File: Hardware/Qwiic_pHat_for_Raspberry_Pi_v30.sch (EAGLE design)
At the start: 28 parts, among them J1 RASPBERRYPI-40-PIN-GPIO_PTH_N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, J4 Qwiic Right Angle, J7 Qwiic Right Angle

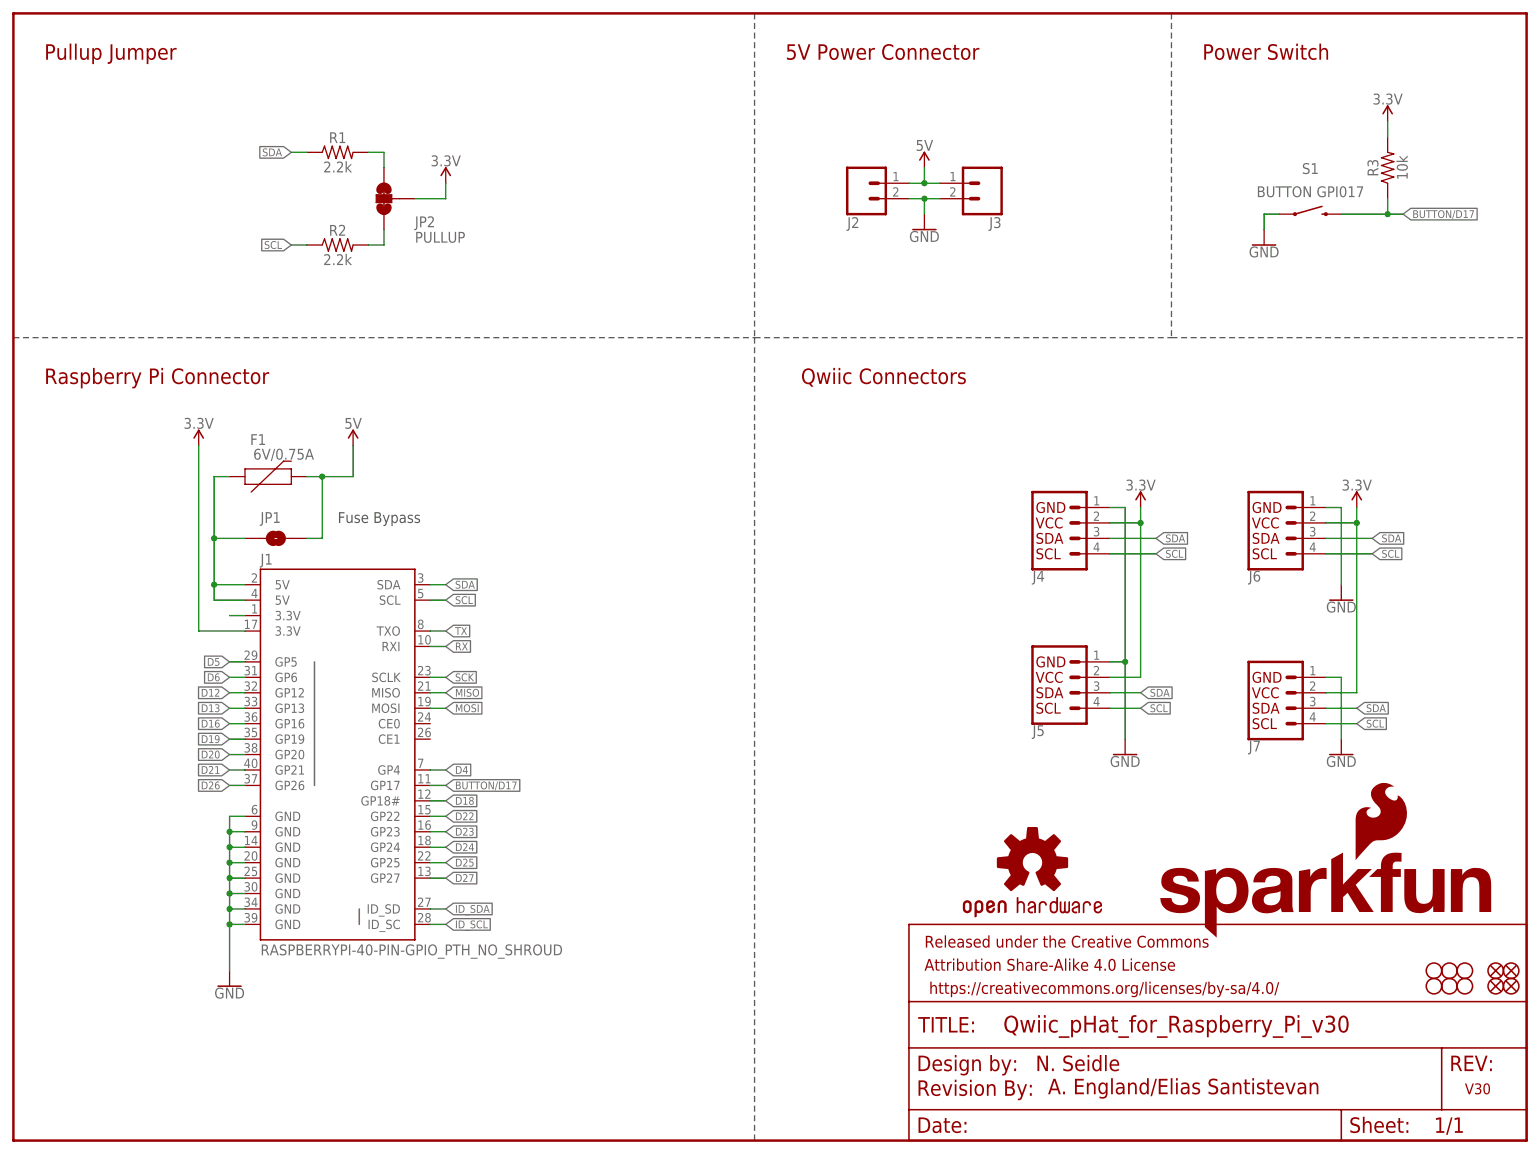
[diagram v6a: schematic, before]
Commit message: Swaps power and ground on screw terminal, adjusts silk in various areas
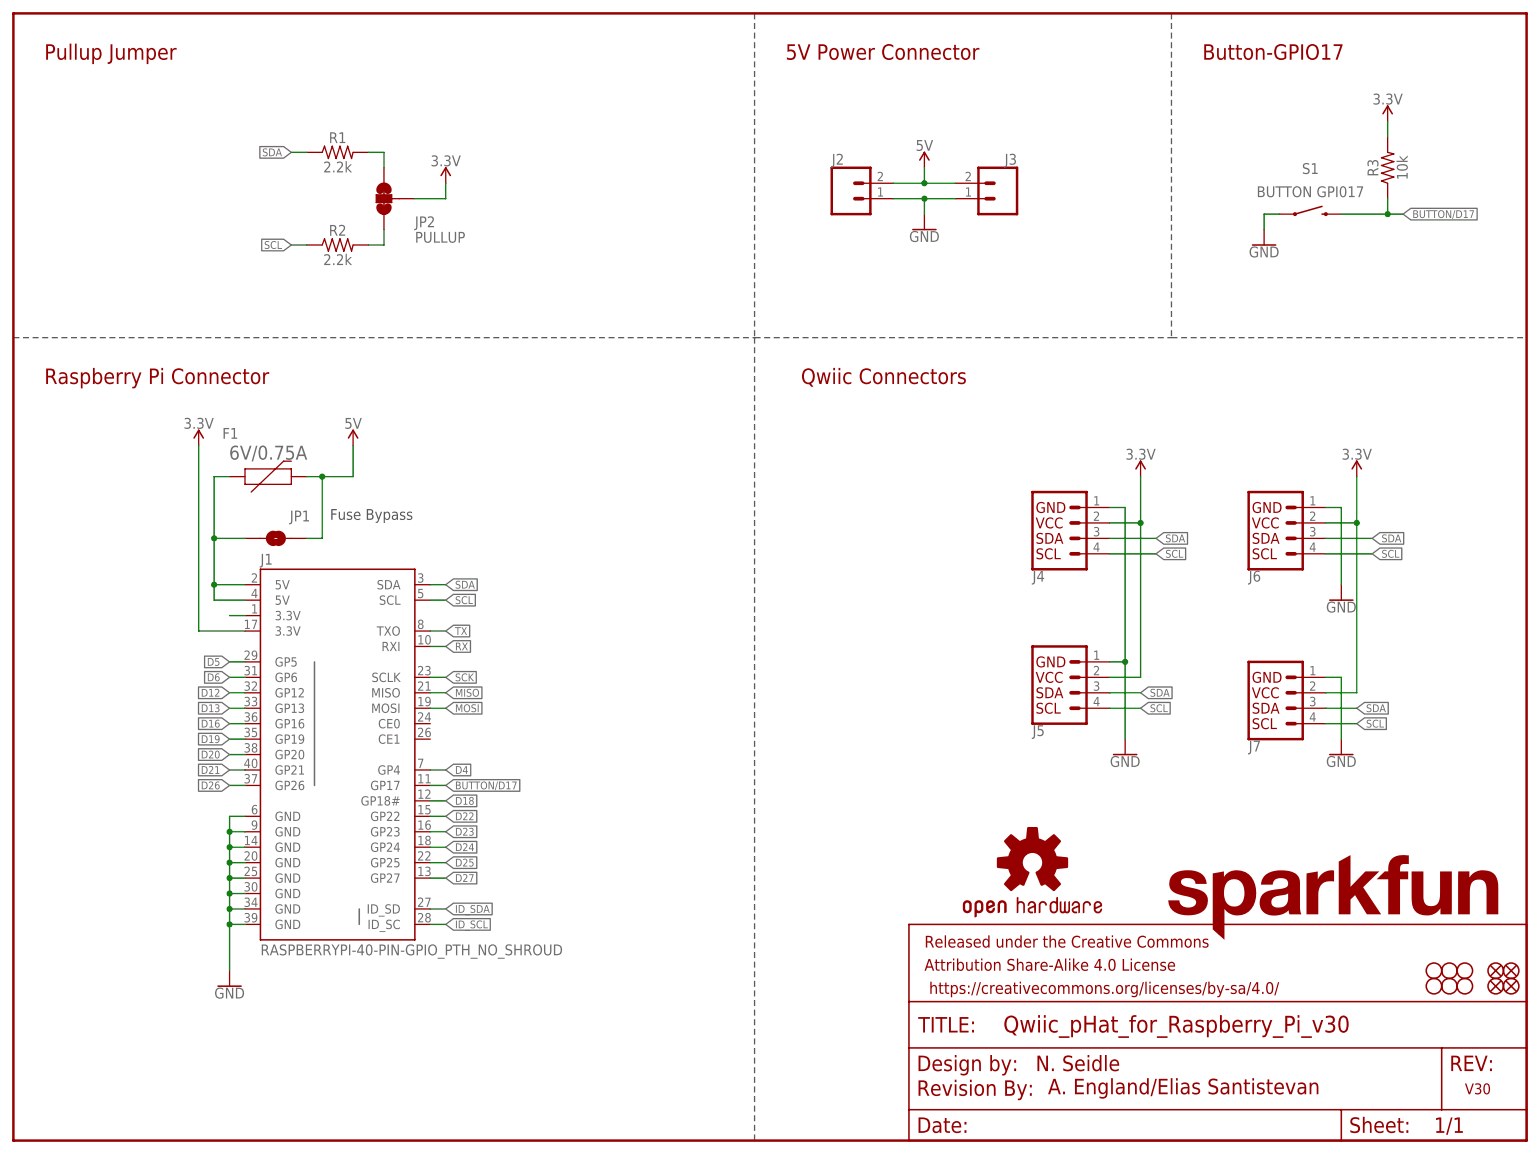
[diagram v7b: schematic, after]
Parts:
- LOGO3: value SFE_LOGO_NAME_FLAME.1_INCH -> SFE_LOGO_NAME.1_INCH; device SparkFun-Aesthetics:SFE_LOGO_NAME_FLAME.1_INCH -> SparkFun-Aesthetics:SFE_LOGO_NAME.1_INCH
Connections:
- net 5V: now also J2.2, J3.2; no longer J2.1, J3.1
- net GND: now also J2.1, J3.1; no longer J2.2, J3.2
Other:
- note added: "Button-GPIO17"
- note removed: "Power Switch"
- moved on the sheet: J2, J3
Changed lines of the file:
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@@
 <part name="H3" library="SparkFun-Hardware" deviceset="STAND-OFF" device="TIGHT"/>
 <part name="H2" library="SparkFun-Hardware" deviceset="STAND-OFF" device="TIGHT"/>
-<part name="LOGO3" library="SparkFun-Aesthetics" deviceset="SFE_LOGO_NAME_FLAME" device=".1_INCH" value="SFE_LOGO_NAME_FLAME.1_INCH"/>
 <part name="LOGO2" library="SparkFun-Aesthetics" deviceset="OSHW-LOGO" device="S" value="OSHW-LOGOS"/>
 <part name="JP2" library="SparkFun-Jumpers" deviceset="JUMPER-SMT_3_2-NC_TRACE" device="_NO-SILK" value="PULLUP"/>
@@
 <part name="F1" library="SparkFun-Fuses" deviceset="PPTC" device="_0.75A" value="6V/0.75A"/>
 <part name="JP1" library="SparkFun-Jumpers" deviceset="JUMPER-SMT_2_NO" device="_SILK" value="JUMPER-SMT_2_NO_SILK"/>
+<part name="LOGO3" library="SparkFun-Aesthetics" deviceset="SFE_LOGO_NAME" device=".1_INCH" value="SFE_LOGO_NAME.1_INCH"/>
 </parts>
 <sheets>
@@
 <wire x1="190.5" y1="132.08" x2="248.92" y2="132.08" width="0.2032" layer="97" style="shortdash"/>
 <wire x1="190.5" y1="185.42" x2="190.5" y2="132.08" width="0.2032" layer="97" style="shortdash"/>
-<text x="195.58" y="177.8" size="2.54" layer="94" font="vector" ratio="12">Power Switch</text>
-<text x="53.34" y="101.6" size="1.778" layer="97" font="vector">Fuse Bypass</text>
+<text x="195.58" y="177.8" size="2.54" layer="94" font="vector" ratio="12">Button-GPIO17</text>
+<text x="52.07" y="102.108" size="1.778" layer="97" font="vector">Fuse Bypass</text>
 </plain>
 <instances>
@@
 <attribute name="NAME" x="167.64" y="93.726" size="1.778" layer="95" font="vector" rot="MR180"/>
 </instance>
-<instance part="SUPPLY5" gate="G$1" x="185.42" y="104.14" smashed="yes">
-<attribute name="VALUE" x="185.42" y="106.934" size="1.778" layer="96" align="bottom-center"/>
+<instance part="SUPPLY5" gate="G$1" x="185.42" y="109.22" smashed="yes">
+<attribute name="VALUE" x="185.42" y="112.014" size="1.778" layer="96" align="bottom-center"/>
 </instance>
 <instance part="GND3" gate="1" x="182.88" y="63.5" smashed="yes">
@@
 <instance part="H3" gate="G$1" x="236.22" y="27.94" smashed="yes"/>
 <instance part="H2" gate="G$1" x="233.68" y="25.4" smashed="yes"/>
-<instance part="LOGO3" gate="G$1" x="187.96" y="33.02" smashed="yes"/>
 <instance part="LOGO2" gate="G$1" x="167.64" y="45.72" smashed="yes"/>
 <instance part="JP2" gate="G$1" x="60.96" y="154.94" smashed="yes" rot="R180">
@@
 <attribute name="VALUE" x="30.48" y="117.094" size="1.778" layer="96" align="bottom-center"/>
 </instance>
-<instance part="J3" gate="G$1" x="160.02" y="157.48" smashed="yes" rot="R180">
-<attribute name="VALUE" x="162.56" y="162.306" size="1.778" layer="96" font="vector" rot="R180"/>
-<attribute name="NAME" x="162.56" y="151.892" size="1.778" layer="95" font="vector" rot="R180"/>
+<instance part="J3" gate="G$1" x="162.56" y="154.94" smashed="yes" rot="MR0">
+<attribute name="VALUE" x="165.1" y="150.114" size="1.778" layer="96" font="vector" rot="MR0"/>
+<attribute name="NAME" x="165.1" y="160.528" size="1.778" layer="95" font="vector" rot="MR0"/>
 </instance>
 <instance part="GND2" gate="1" x="149.86" y="149.86" smashed="yes">
@@
 <attribute name="VALUE" x="218.44" y="88.646" size="1.778" layer="96" align="top-center"/>
 </instance>
-<instance part="SUPPLY6" gate="G$1" x="220.98" y="104.14" smashed="yes">
-<attribute name="VALUE" x="220.98" y="106.934" size="1.778" layer="96" align="bottom-center"/>
-</instance>
-<instance part="J2" gate="G$1" x="139.7" y="157.48" smashed="yes" rot="MR180">
-<attribute name="VALUE" x="137.16" y="162.306" size="1.778" layer="96" font="vector" rot="MR180"/>
-<attribute name="NAME" x="137.16" y="151.892" size="1.778" layer="95" font="vector" rot="MR180"/>
+<instance part="SUPPLY6" gate="G$1" x="220.98" y="109.22" smashed="yes">
+<attribute name="VALUE" x="220.98" y="112.014" size="1.778" layer="96" align="bottom-center"/>
+</instance>
+<instance part="J2" gate="G$1" x="137.16" y="154.94" smashed="yes">
+<attribute name="VALUE" x="134.62" y="150.114" size="1.778" layer="96" font="vector"/>
+<attribute name="NAME" x="134.62" y="160.528" size="1.778" layer="95" font="vector"/>
 </instance>
 <instance part="F1" gate="F1" x="40.64" y="109.22" smashed="yes">
-<attribute name="NAME" x="40.259" y="116.205" size="1.778" layer="95" font="vector" rot="R180" align="bottom-center"/>
-<attribute name="VALUE" x="44.45" y="112.014" size="1.778" layer="96" font="vector" rot="R180" align="top-center"/>
+<attribute name="NAME" x="35.687" y="117.221" size="1.778" layer="95" font="vector" rot="R180" align="bottom-center"/>
+<attribute name="VALUE" x="41.91" y="112.014" size="2.286" layer="96" font="vector" rot="R180" align="top-center"/>
 </instance>
 <instance part="JP1" gate="G$1" x="43.18" y="99.06" smashed="yes">
-<attribute name="NAME" x="40.64" y="101.6" size="1.778" layer="95" font="vector"/>
-</instance>
+<attribute name="NAME" x="45.466" y="101.854" size="1.778" layer="95" font="vector"/>
+</instance>
+<instance part="LOGO3" gate="G$1" x="187.96" y="33.02" smashed="yes"/>
 </instances>
 <busses>
@@
 </segment>
 <segment>
-<pinref part="J3" gate="G$1" pin="2"/>
-<wire x1="152.4" y1="154.94" x2="149.86" y2="154.94" width="0.1524" layer="91"/>
-<wire x1="149.86" y1="154.94" x2="149.86" y2="152.4" width="0.1524" layer="91"/>
-<pinref part="GND2" gate="1" pin="GND"/>
-<pinref part="J2" gate="G$1" pin="2"/>
-<wire x1="147.32" y1="154.94" x2="149.86" y2="154.94" width="0.1524" layer="91"/>
-<junction x="149.86" y="154.94"/>
-</segment>
-<segment>
 <pinref part="S1" gate="G$1" pin="1"/>
 <wire x1="208.28" y1="152.4" x2="205.74" y2="152.4" width="0.1524" layer="91"/>
@@
 <pinref part="GND5" gate="1" pin="GND"/>
 </segment>
+<segment>
+<pinref part="J3" gate="G$1" pin="1"/>
+<pinref part="J2" gate="G$1" pin="1"/>
+<wire x1="144.78" y1="154.94" x2="149.86" y2="154.94" width="0.1524" layer="91"/>
+<wire x1="149.86" y1="154.94" x2="154.94" y2="154.94" width="0.1524" layer="91"/>
+<wire x1="149.86" y1="154.94" x2="149.86" y2="152.4" width="0.1524" layer="91"/>
+<junction x="149.86" y="154.94"/>
+<pinref part="GND2" gate="1" pin="GND"/>
+</segment>
 </net>
 <net name="3.3V" class="0">
@@
 <pinref part="J4" gate="G$1" pin="2"/>
 <wire x1="180.34" y1="101.6" x2="185.42" y2="101.6" width="0.1524" layer="91"/>
-<wire x1="185.42" y1="101.6" x2="185.42" y2="104.14" width="0.1524" layer="91"/>
+<wire x1="185.42" y1="101.6" x2="185.42" y2="109.22" width="0.1524" layer="91"/>
 <pinref part="SUPPLY5" gate="G$1" pin="3.3V"/>
 <pinref part="J5" gate="G$1" pin="2"/>
@@
 <pinref part="J6" gate="G$1" pin="2"/>
 <wire x1="215.9" y1="101.6" x2="220.98" y2="101.6" width="0.1524" layer="91"/>
-<wire x1="220.98" y1="101.6" x2="220.98" y2="104.14" width="0.1524" layer="91"/>
+<wire x1="220.98" y1="101.6" x2="220.98" y2="109.22" width="0.1524" layer="91"/>
 <pinref part="SUPPLY6" gate="G$1" pin="3.3V"/>
 <pinref part="J7" gate="G$1" pin="2"/>
@@
 </net>
 <net name="5V" class="0">
-<segment>
-<pinref part="J3" gate="G$1" pin="1"/>
-<wire x1="152.4" y1="157.48" x2="149.86" y2="157.48" width="0.1524" layer="91"/>
-<wire x1="149.86" y1="157.48" x2="149.86" y2="160.02" width="0.1524" layer="91"/>
-<pinref part="SUPPLY4" gate="G$1" pin="5V"/>
-<pinref part="J2" gate="G$1" pin="1"/>
-<wire x1="147.32" y1="157.48" x2="149.86" y2="157.48" width="0.1524" layer="91"/>
-<junction x="149.86" y="157.48"/>
-</segment>
 <segment>
 <pinref part="F1" gate="F1" pin="2"/>
@@
 <wire x1="55.88" y1="109.22" x2="55.88" y2="114.3" width="0.1524" layer="91"/>
 </segment>
-</net>
+<segment>
+<pinref part="J3" gate="G$1" pin="2"/>
+<pinref part="J2" gate="G$1" pin="2"/>
+<wire x1="144.78" y1="157.48" x2="149.86" y2="157.48" width="0.1524" layer="91"/>
+<pinref part="SUPPLY4" gate="G$1" pin="5V"/>
+<wire x1="149.86" y1="157.48" x2="154.94" y2="157.48" width="0.1524" layer="91"/>
+<wire x1="149.86" y1="157.48" x2="149.86" y2="160.02" width="0.1524" layer="91"/>
+<junction x="149.86" y="157.48"/>
+</segment>
+</net>
